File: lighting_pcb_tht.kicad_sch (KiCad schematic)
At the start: 20 parts, among them J1 Screw_Terminal_01x03, SW1 SW_Push, SW2 SW_Push, SW3 SW_Push, U1 ATmega328-P, Y1 Crystal

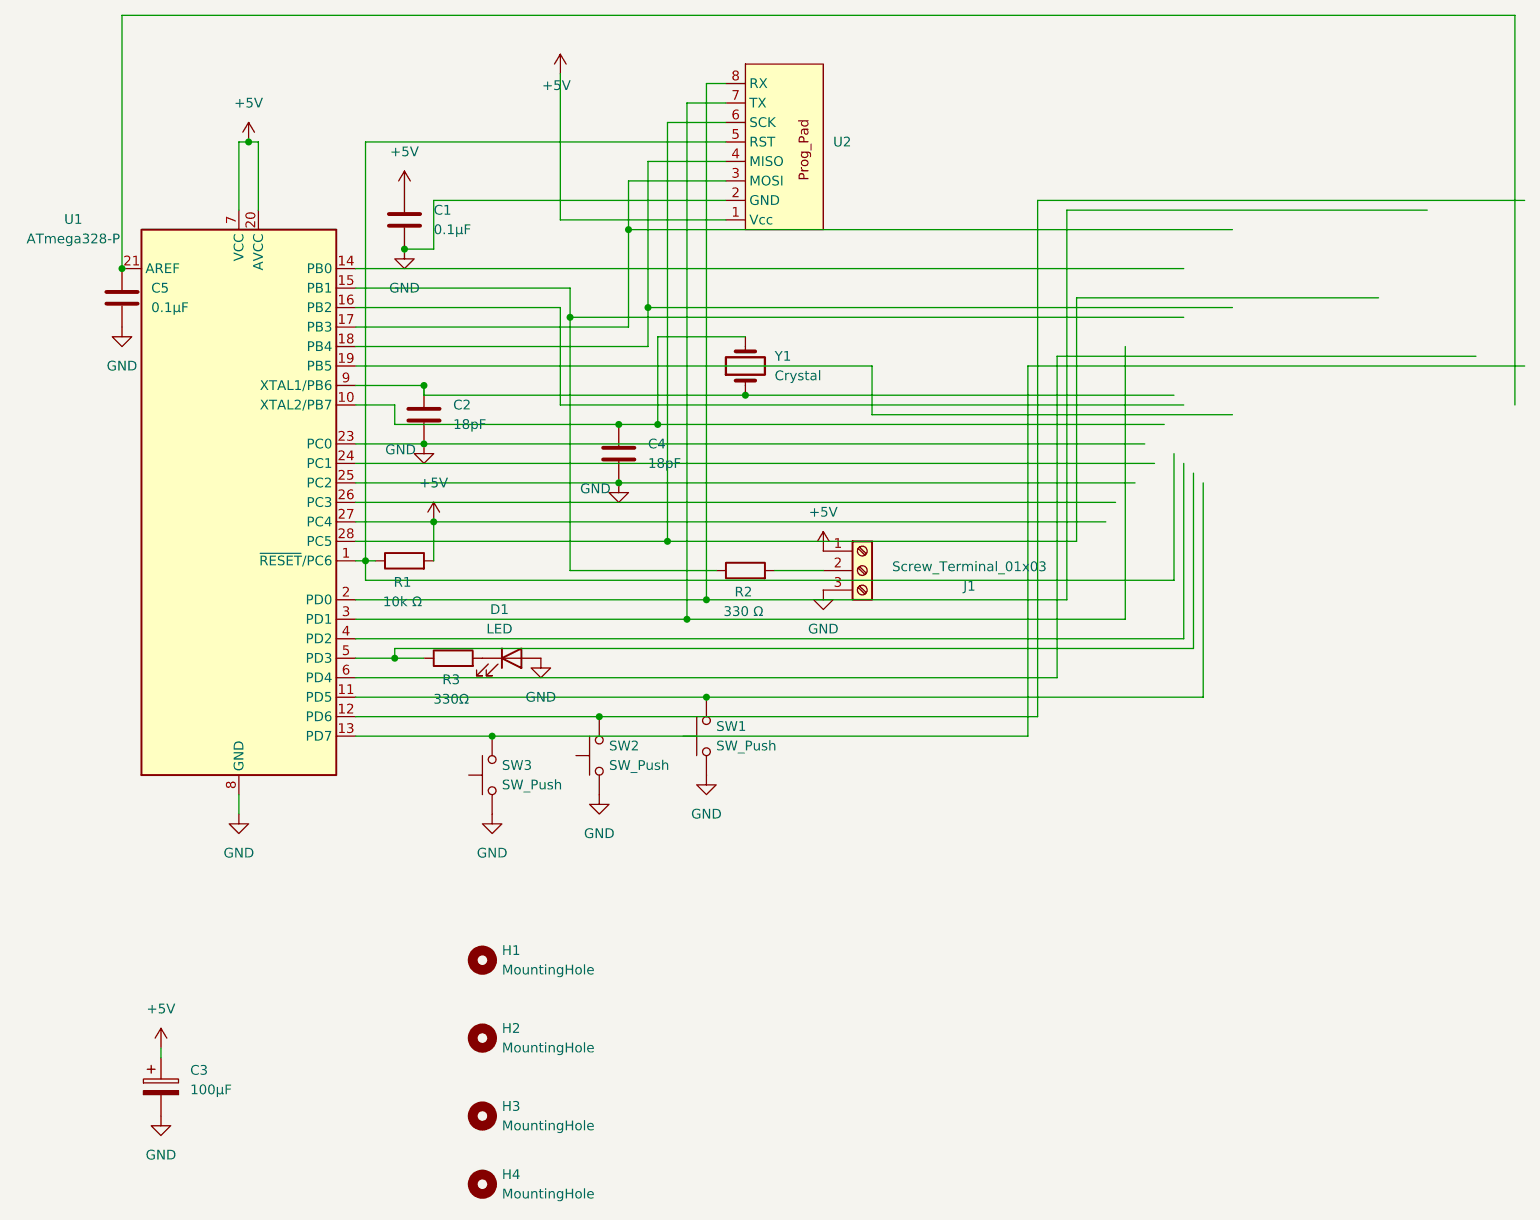
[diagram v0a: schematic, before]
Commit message: Changed the pads used for programming to header pins
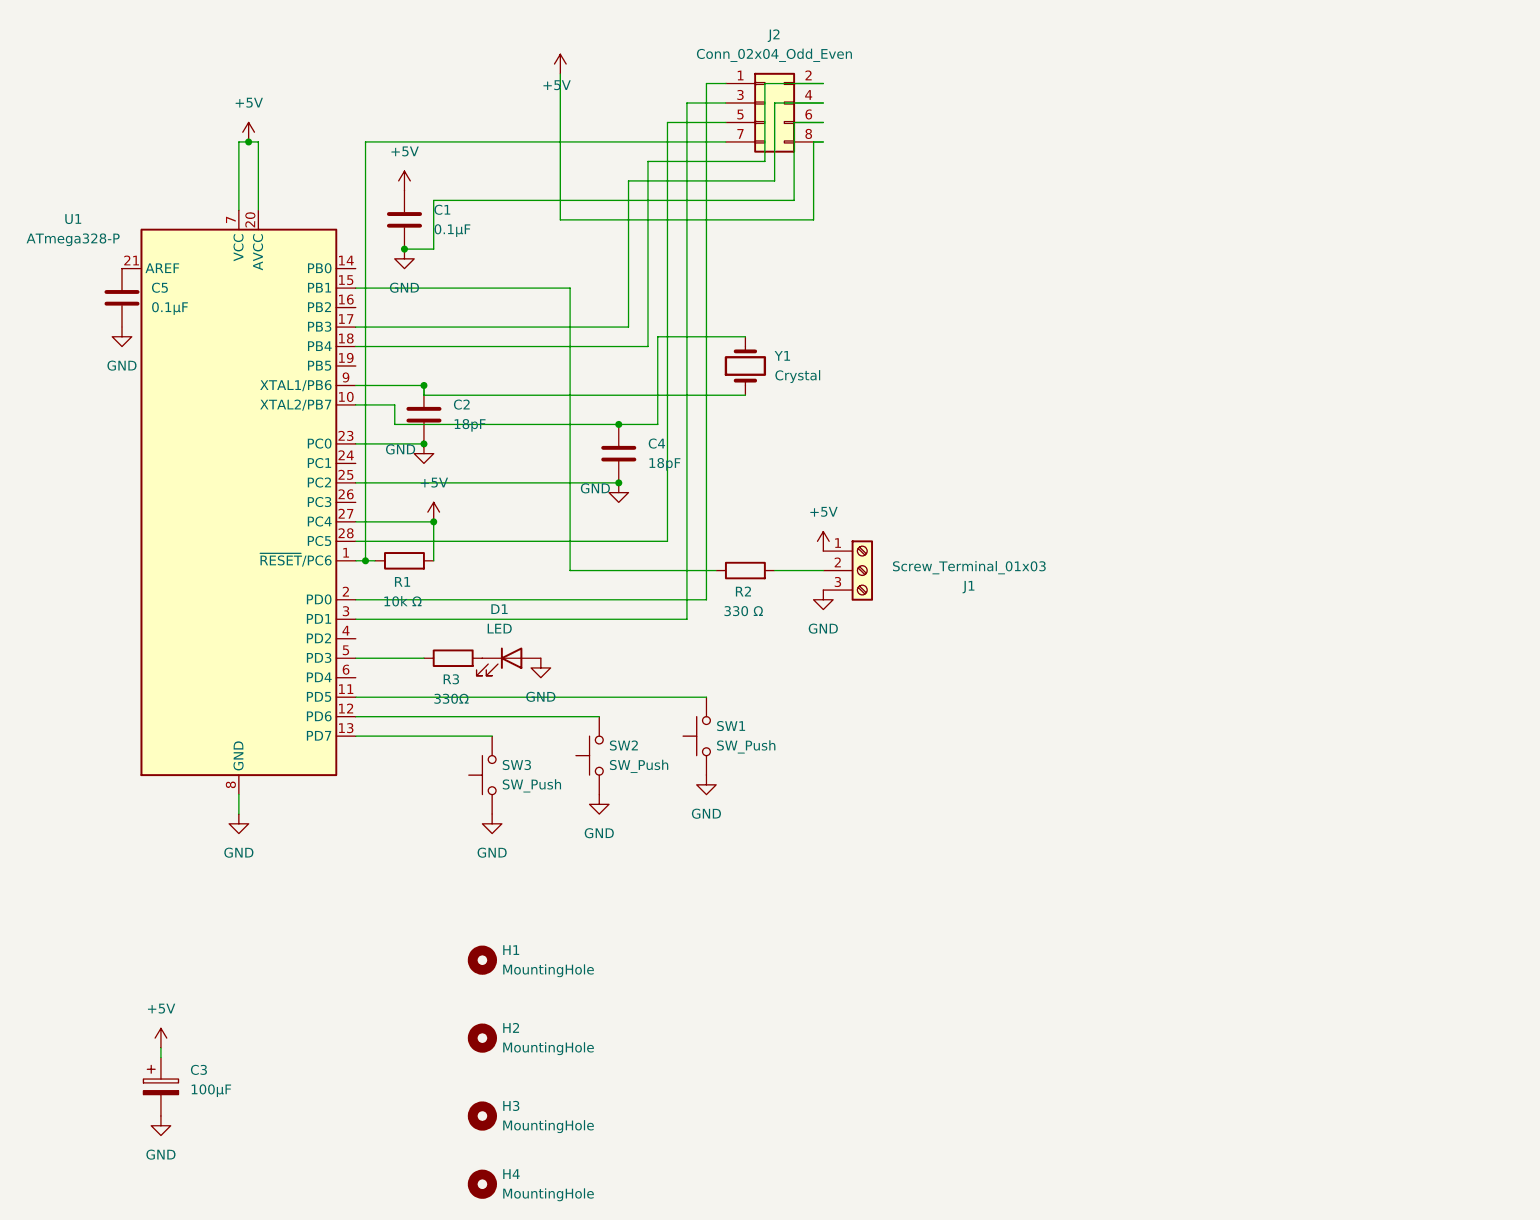
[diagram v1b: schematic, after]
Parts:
- removed U2: ~, Programming_Pad:Programming_Pad, symbol pad_lib:Programming_Pad
- added J2: Conn_02x04_Odd_Even, Connector_PinHeader_2.54mm:PinHeader_2x04_P2.54mm_Vertical, symbol Connector_Generic:Conn_02x04_Odd_Even
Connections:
- net +5V: now also J2.8 (Pin_8)
- net GND: now also J2.6 (Pin_6)
- net at R1.1, U1.1 (~{RESET}/PC6): now also J2.7 (Pin_7)
- net at U1.17 (PB3): now also J2.4 (Pin_4)
- net at U1.18 (PB4): now also J2.2 (Pin_2)
- net at U1.2 (PD0): now also J2.1 (Pin_1)
- net at U1.28 (PC5): now also J2.5 (Pin_5)
- net at U1.3 (PD1): now also J2.3 (Pin_3)

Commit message: Final design with THT chip and SMD res/caps
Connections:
- net +5V: now also J1.3 (Pin_3); no longer J1.1 (Pin_1), U1.27 (PC4)
- net GND: now also J1.1 (Pin_1); no longer J1.3 (Pin_3)
- net at J2.5 (Pin_5): now also U1.19 (PB5); no longer U1.28 (PC5)
- no-connect marks 0 -> 8
